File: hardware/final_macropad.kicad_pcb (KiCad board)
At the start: 4 copper layers, 91 x 91.8 mm, 65 parts, among them J1 OLED_128x64, SW1 SW_Push, U1 ATmega32U4-A, Y1 16MHz

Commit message: organize schematic and add USB-C and surge protector
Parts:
- removed R2, R3: 22, Resistor_SMD:R_0402_1005Metric_Pad0.72x0.64mm_HandSolder
- removed USB1: Molex-0548190589, random-keyboard-parts:Molex-0548190589
- added C10: 100nF, Capacitor_SMD:C_0805_2012Metric, F.Cu at (237.7, 42.0)
- added C11: 100nF, Capacitor_SMD:C_0805_2012Metric, F.Cu at (237.7, 45.1)
- added C8: 100nF, Capacitor_SMD:C_0805_2012Metric, F.Cu at (237.7, 36.0)
- added C9: 100nF, Capacitor_SMD:C_0805_2012Metric, F.Cu at (237.7, 39.0)
- added D1: SOD-123, Diode_SMD:D_SOD-123, F.Cu at (231.6, 101.7)
- added D10: SOD-123, Diode_SMD:D_SOD-123, F.Cu at (237.3, 111.8)
- added D11: SOD-123, Diode_SMD:D_SOD-123, F.Cu at (237.3, 115.1)
- added D12: SOD-123, Diode_SMD:D_SOD-123, F.Cu at (237.3, 118.5)
- added D13: SOD-123, Diode_SMD:D_SOD-123, F.Cu at (243.1, 101.7)
- added D14: SOD-123, Diode_SMD:D_SOD-123, F.Cu at (243.1, 105.0)
- added D15: SOD-123, Diode_SMD:D_SOD-123, F.Cu at (243.1, 108.4)
- added D16: SOD-123, Diode_SMD:D_SOD-123, F.Cu at (243.1, 111.8)
- added D2: SOD-123, Diode_SMD:D_SOD-123, F.Cu at (231.6, 105.0)
- added D3: SOD-123, Diode_SMD:D_SOD-123, F.Cu at (231.6, 108.4)
- added D4: SOD-123, Diode_SMD:D_SOD-123, F.Cu at (231.6, 111.8)
- added D5: SOD-123, Diode_SMD:D_SOD-123, F.Cu at (231.6, 115.1)
- added D6: SOD-123, Diode_SMD:D_SOD-123, F.Cu at (231.6, 118.5)
- added D7: SOD-123, Diode_SMD:D_SOD-123, F.Cu at (237.3, 101.7)
- added D8: SOD-123, Diode_SMD:D_SOD-123, F.Cu at (237.3, 105.0)
- added D9: SOD-123, Diode_SMD:D_SOD-123, F.Cu at (237.3, 108.4)
- added H10: OLED_Mount, MountingHole:MountingHole_2.2mm_M2_Pad, F.Cu at (228.1, 43.5)
- added H11: OLED_Mount, MountingHole:MountingHole_2.2mm_M2_Pad, F.Cu at (228.1, 49.4)
- added H12: OLED_Mount, MountingHole:MountingHole_2.2mm_M2_Pad, F.Cu at (228.1, 55.4)
- added H9: OLED_Mount, MountingHole:MountingHole_2.2mm_M2_Pad, F.Cu at (228.1, 37.5)
- added J2: 2137160001, kicad-footprints:MOLEX_2137160001, F.Cu at (138.1, 39.5)
- added J2: 2137160001, kicad-footprints:MOLEX_2137160001, F.Cu at (88.7, 25.9)
- added R10: 10k, Resistor_SMD:R_0805_2012Metric, F.Cu at (233.2, 50.8)
- added R11: 5.1k, Resistor_SMD:R_0805_2012Metric, F.Cu at (134.5, 42.2)
- added R11: 5.1k, Resistor_SMD:R_0805_2012Metric, F.Cu at (77.8, 30.0)
- added R12: 5.1k, Resistor_SMD:R_0805_2012Metric, F.Cu at (134.5, 45.2)
- added R12: 5.1k, Resistor_SMD:R_0805_2012Metric, F.Cu at (77.8, 33.0)
- added R5: 27k, Resistor_SMD:R_0805_2012Metric, F.Cu at (233.2, 36.0)
- added R6: 27k, Resistor_SMD:R_0805_2012Metric, F.Cu at (233.2, 39.0)
- added R7: 10k, Resistor_SMD:R_0805_2012Metric, F.Cu at (233.2, 41.9)
- added R8: 27k, Resistor_SMD:R_0805_2012Metric, F.Cu at (233.2, 44.9)
- added R9: 27k, Resistor_SMD:R_0805_2012Metric, F.Cu at (233.2, 47.8)
- added S15: Keyswitch, Button_Switch_Keyboard:SW_Cherry_MX_1.00u_PCB, F.Cu at (105.5, 64.8)
- added S16: Keyswitch, Button_Switch_Keyboard:SW_Cherry_MX_1.00u_PCB, F.Cu at (105.5, 84.0)
- added S17: Keyswitch, Button_Switch_Keyboard:SW_Cherry_MX_1.00u_PCB, F.Cu at (105.5, 103.2)
- added S18: Keyswitch, Button_Switch_Keyboard:SW_Cherry_MX_1.00u_PCB, F.Cu at (105.5, 122.5)
- added U2: USBLC6-2SC6, kicad-footprints:SOT95P280X145-6N, F.Cu at (140.0, 43.0)
- added U2: USBLC6-2SC6, kicad-footprints:SOT95P280X145-6N, F.Cu at (68.3, 33.5)
- F1: moved to F.Cu
- H1, H2, H3, H4, H5, H6, H7, H8: value MountingHole_Pad -> MountHole
- S13: footprint PEC16-4220F-S0024:PEC16-4xxxx-Sxxxx -> kicad-footprints:PEC16-4xxxx-Sxxxx
- moved F1 82.8 mm to (145.4, 42.4), turned to 0 degrees
- moved S4 82.5 mm to (47.8, 122.5)
- moved S14 81.6 mm to (155.2, 66.8)
- moved S13 80.6 mm to (179.5, 65.5)
- moved S8 55.3 mm to (67.0, 122.5)
- moved S3 55.2 mm to (47.8, 103.2)
- moved S9 53.8 mm to (86.2, 64.8)
- moved J1 39.3 mm to (10.4, 26.8)
- moved S7 28.0 mm to (67.0, 103.2)
- moved S12 28.0 mm to (86.2, 122.5)
- moved S2 28.0 mm to (47.8, 84.0)
- moved S5 26.5 mm to (67.0, 64.8)
- moved S10 26.5 mm to (86.2, 84.0)
- moved H3 25.8 mm to (32.5, 140.1)
- moved H4 25.8 mm to (114.5, 140.1)
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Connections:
- U1 pad 27: unconnected-(U1-PD7-Pad27) -> ROW 3
- U1 pad 3: /CAPD- -> MPU_USB_D-
- U1 pad 4: /CAPD+ -> MPU_USB_D+
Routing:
- net COL 2: track 83.3 -> 44.7 mm
- net COL 0: track 57.4 -> 18.9 mm
- net COL 3: track 101.4 -> 62.9 mm
- net COL 1: track 66.5 -> 28.1 mm
- net /CAPD+: track 16.8 -> 0.00 mm
- net /CAPD-: track 16.8 -> 0.00 mm
- net Net-(D5-A): track 14.3 -> 0.00 mm
- net 5V: track 33.9 -> 27.2 mm, vias 7 -> 6
- net VCC: track 5.24 -> 0.00 mm
- net D+: track 2.91 -> 0.00 mm
- net D-: track 2.89 -> 0.00 mm
- net ROW 1: track 105.4 -> 102.9 mm
- net GND: track 51.0 -> 50.7 mm, vias 12 -> 10
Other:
- board size 91 x 91.8 mm -> 91.2 x 118 mm

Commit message: remove old diodes
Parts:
- removed the D1 at (54.8, 67.5)
- removed the D10 at (74.0, 107.2)
- removed the D11 at (93.2, 107.2)
- removed the D12 at (112.8, 107.2)
- removed the D2 at (73.8, 67.5)
- removed the D3 at (93.0, 67.5)
- removed the D4 at (112.5, 67.5)
- removed the D5 at (54.5, 89.2)
- removed the D6 at (73.8, 89.2)
- removed the D7 at (93.2, 89.2)
- removed the D8 at (112.5, 89.2)
- removed the D9 at (54.5, 107.2)
- moved D1 230.0 mm to (5.05, 61.5)
- moved D10 230.0 mm to (10.8, 71.6)
- moved D11 230.0 mm to (10.8, 75.0)
- moved D12 230.0 mm to (10.8, 78.3)
- moved D13 230.0 mm to (16.6, 61.5)
- moved D14 230.0 mm to (16.6, 64.9)
- moved D15 230.0 mm to (16.6, 68.2)
- moved D16 230.0 mm to (16.6, 71.6)
- moved D2 230.0 mm to (5.05, 64.9)
- moved D3 230.0 mm to (5.05, 68.2)
- moved D4 230.0 mm to (5.05, 71.6)
- moved D5 230.0 mm to (5.05, 75.0)
- moved D6 230.0 mm to (5.05, 78.3)
- moved D7 230.0 mm to (10.8, 61.5)
- moved D8 230.0 mm to (10.8, 64.9)
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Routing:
- net COL 0: track 18.9 -> 32.5 mm
- net Net-(D1-A): track 13.7 -> 0.00 mm

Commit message: fix switches to be correct order and move diodes
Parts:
- D1, D10, D11, D12, D13, D14, D15, D16, D2, D3, D4, D5, D6, D7, D8, D9: moved to B.Cu
- H5, H6, H7, H8: footprint MountingHole:MountingHole_3.2mm_M3_Pad_Via -> MountingHole:MountingHole_2.2mm_M2_Pad
- moved D16 110.8 mm to (112.5, 127.2), turned to 90 degrees
- moved D4 107.5 mm to (112.5, 68.5), turned to 90 degrees
- moved D12 105.9 mm to (112.5, 107.8), turned to 90 degrees
- moved D8 104.2 mm to (112.5, 88.0), turned to 90 degrees
- moved D15 96.9 mm to (93.5, 127.2), turned to 90 degrees
- moved D11 88.7 mm to (93.2, 107.8), turned to 90 degrees
- moved D3 88.4 mm to (93.5, 68.5), turned to 90 degrees
- moved D7 86.8 mm to (93.5, 88.0), turned to 90 degrees
- moved D14 84.9 mm to (74.2, 127.2), turned to 90 degrees
- moved C10 84.3 mm to (156.1, 63.2)
- moved C11 84.3 mm to (156.1, 66.2)
- moved C8 84.3 mm to (156.1, 57.2)
- moved C9 84.3 mm to (156.1, 60.2)
- moved H10 84.3 mm to (146.5, 64.6)
- moved H11 84.3 mm to (146.5, 70.5)
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- renumbered S15 to S13, S16 to S14, S17 to S15, S18 to S16, S13 to S17, S14 to S18
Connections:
- R5 pad 2: Net-(S13-CHANNEL_A) -> Net-(S17-CHANNEL_A)
- R6 pad 2: Net-(S13-CHANNEL_B) -> Net-(S17-CHANNEL_B)
- R8 pad 2: Net-(S14-CHANNEL_A) -> Net-(S18-CHANNEL_A)
- R9 pad 2: Net-(S14-CHANNEL_B) -> Net-(S18-CHANNEL_B)
- S17 pad A: Net-(S13-CHANNEL_A) -> Net-(S17-CHANNEL_A)
- S17 pad B: Net-(S13-CHANNEL_B) -> Net-(S17-CHANNEL_B)
- S18 pad A: Net-(S14-CHANNEL_A) -> Net-(S18-CHANNEL_A)
- S18 pad B: Net-(S14-CHANNEL_B) -> Net-(S18-CHANNEL_B)
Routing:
- net ROW 2: track 141.0 -> 37.7 mm, vias 2 -> 1
- net ROW 1: track 102.9 -> 19.9 mm, vias 2 -> 1
- net ROW 0: track 92.0 -> 19.6 mm, vias 2 -> 1
- net Net-(D7-A): track 14.5 -> 0.00 mm
- net SDA: track 18.2 -> 3.70 mm
- net Net-(D8-A): track 14.5 -> 0.00 mm
- net Net-(D6-A): track 14.3 -> 0.00 mm
- net Net-(D12-A): track 14.2 -> 0.00 mm
- net Net-(D10-A): track 14.0 -> 0.00 mm
- net Net-(D11-A): track 13.9 -> 0.00 mm
- net Net-(D9-A): track 13.8 -> 0.00 mm
- net COL 0: track 32.5 -> 18.9 mm
- net Net-(D4-A): track 13.6 -> 0.00 mm
- net Net-(D2-A): track 13.4 -> 0.00 mm
- net Net-(D3-A): track 13.3 -> 0.00 mm
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
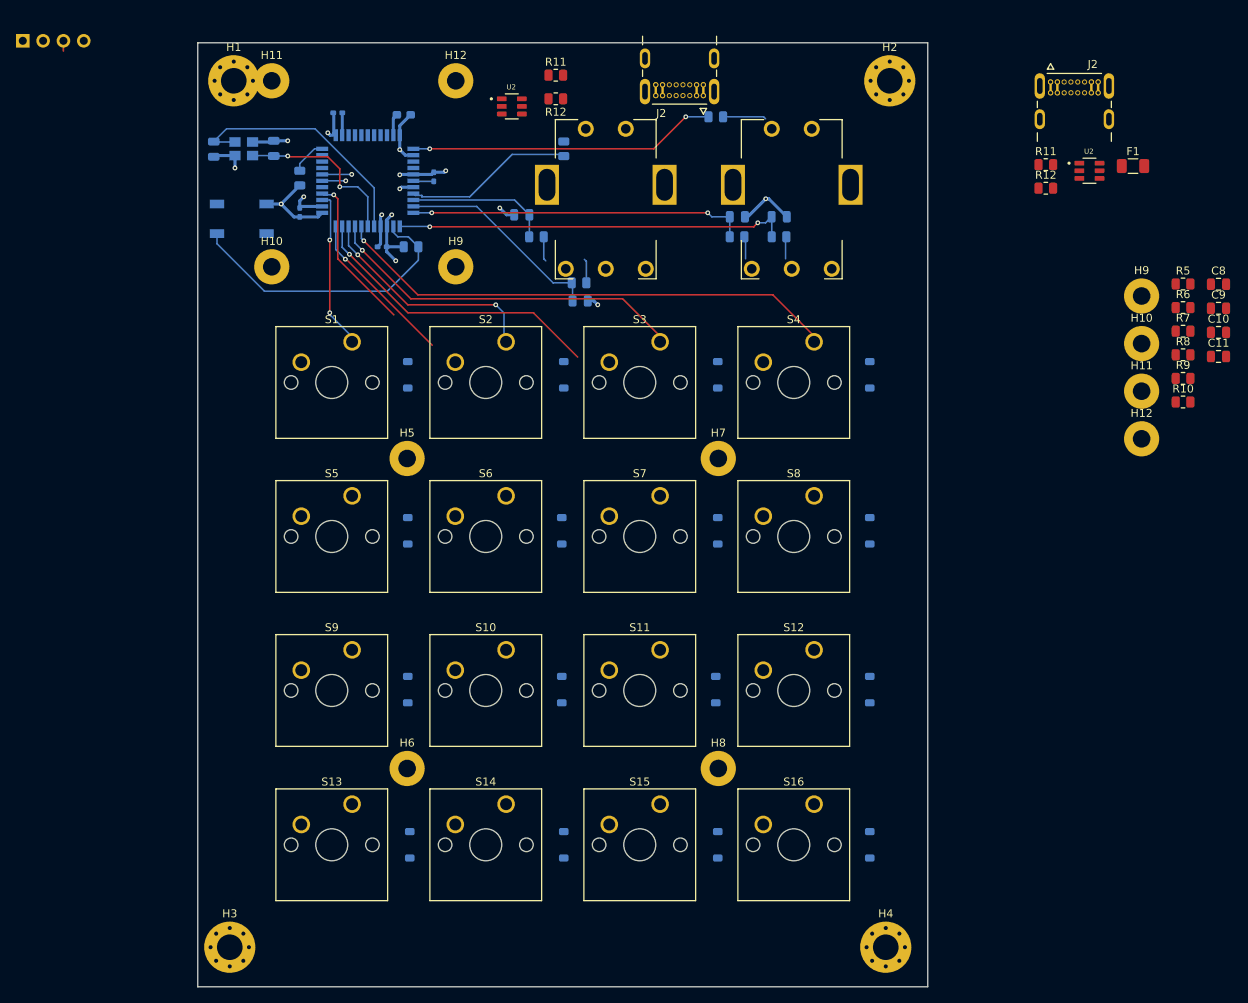
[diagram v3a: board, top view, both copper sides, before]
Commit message: route USBC connector
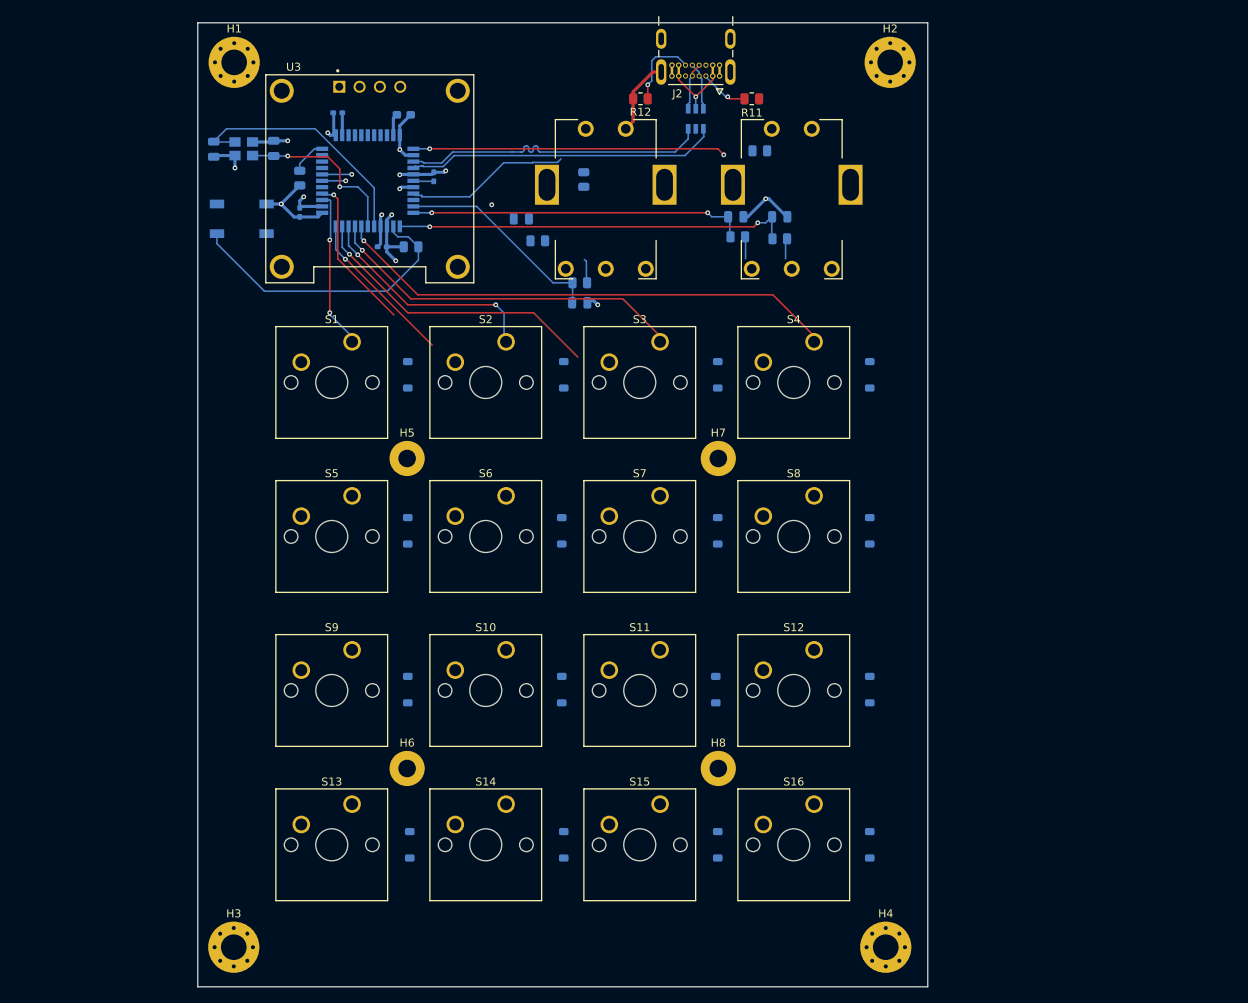
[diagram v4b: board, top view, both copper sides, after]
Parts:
- removed the C10 at (156.1, 63.2)
- removed the C10 at (69.0, 48.5)
- removed the C11 at (156.1, 66.2)
- removed the C11 at (76.3, 59.2)
- removed the C8 at (156.1, 57.2)
- removed the C8 at (96.0, 48.8)
- removed the C9 at (156.1, 60.2)
- removed the C9 at (101.2, 48.8)
- removed F1: 500mA, Fuse:Fuse_1206_3216Metric
- removed H10 (x2), H11 (x2), H12 (x2), H9 (x2): OLED_Mount, MountingHole:MountingHole_2.2mm_M2_Pad
- removed J1: OLED_128x64, ScottoKeebs_Components:OLED_128x64
- removed the J2 at (138.1, 39.5)
- removed the J2 at (88.7, 25.9)
- removed the R10 at (151.7, 71.9)
- removed the R10 at (74.2, 40.2)
- removed the R11 at (134.5, 42.2)
- removed the R11 at (73.2, 31.1)
- removed the R12 at (134.5, 45.2)
- removed the R12 at (73.2, 34.0)
- removed the R5 at (151.7, 57.1)
- removed the R5 at (95.9, 51.2)
- removed the R6 at (151.7, 60.1)
- removed the R6 at (101.2, 51.2)
- removed the R7 at (151.7, 63.0)
- removed the R7 at (93.2, 36.2)
- removed the R8 at (151.7, 66.0)
- removed the R8 at (70.8, 51.2)
- removed the R9 at (151.7, 69.0)
- removed the R9 at (76.2, 57.0)
- removed the U2 at (140.0, 43.0)
- removed the U2 at (67.8, 35.0)
- added C10: 100nF, Capacitor_SMD:C_0805_2012Metric, B.Cu at (69.0, 49.0)
- added C11: 100nF, Capacitor_SMD:C_0805_2012Metric, B.Cu at (76.2, 59.5)
- added C8: 100nF, Capacitor_SMD:C_0805_2012Metric, B.Cu at (95.8, 48.8)
- added C9: 100nF, Capacitor_SMD:C_0805_2012Metric, B.Cu at (101.2, 48.8)
- added J2: 2137160001, kicad-footprints:MOLEX_2137160001, F.Cu at (90.8, 23.5)
- added R10: 10k, Resistor_SMD:R_0805_2012Metric, B.Cu at (76.8, 44.1)
- added R11: 5.1k, Resistor_SMD:R_0805_2012Metric, F.Cu at (97.8, 34.0)
- added R12: 5.1k, Resistor_SMD:R_0805_2012Metric, F.Cu at (83.8, 34.0)
- added R5: 27k, Resistor_SMD:R_0805_2012Metric, B.Cu at (96.0, 51.2)
- added R6: 27k, Resistor_SMD:R_0805_2012Metric, B.Cu at (101.2, 51.5)
- added R7: 10k, Resistor_SMD:R_0805_2012Metric, B.Cu at (98.8, 40.5)
- added R8: 27k, Resistor_SMD:R_0805_2012Metric, B.Cu at (71.0, 51.8)
- added R9: 27k, Resistor_SMD:R_0805_2012Metric, B.Cu at (76.2, 57.0)
- added U2: USBLC6-2SC6, kicad-footprints:SOT95P280X145-6N, B.Cu at (90.8, 36.5)
- added U3: DM-OLED096-636, kicad-footprints:MODULE_DM-OLED096-636, F.Cu at (50.0, 44.0)
- moved H1 2.30 mm to (33.1, 29.4)
- moved H2 2.30 mm to (115.1, 29.4)
- moved H3 0.50 mm to (33.0, 140.1)
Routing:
- net MPU_USB_D+: track 0.00 -> 39.1 mm
- net MPU_USB_D-: track 0.00 -> 39.0 mm
- net ROTA1: track 18.0 -> 0.00 mm
- net ROTB0: track 49.5 -> 59.4 mm, vias 2 -> 3
- net Net-(J2-CC2): track 0.00 -> 9.86 mm, vias 0 -> 1
- net VBUS+: track 0.00 -> 8.46 mm, vias 0 -> 2
- net Net-(J2-CC1): track 0.00 -> 6.07 mm, vias 0 -> 1
- net USB_D+: track 0.00 -> 6.01 mm
- net USB_D-: track 0.00 -> 6.01 mm
- net Net-(R7-Pad2): track 5.42 -> 0.00 mm
- net Net-(S14-CHANNEL_A): track 3.10 -> 0.00 mm
- net Net-(S18-CHANNEL_B): track 0.00 -> 3.03 mm
- net Net-(S14-CHANNEL_B): track 3.03 -> 0.00 mm
- net Net-(S17-CHANNEL_A): track 0.00 -> 2.81 mm
- net Net-(S13-CHANNEL_A): track 2.81 -> 0.00 mm
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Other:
- board size 91.2 x 118 mm -> 91.2 x 120.5 mm

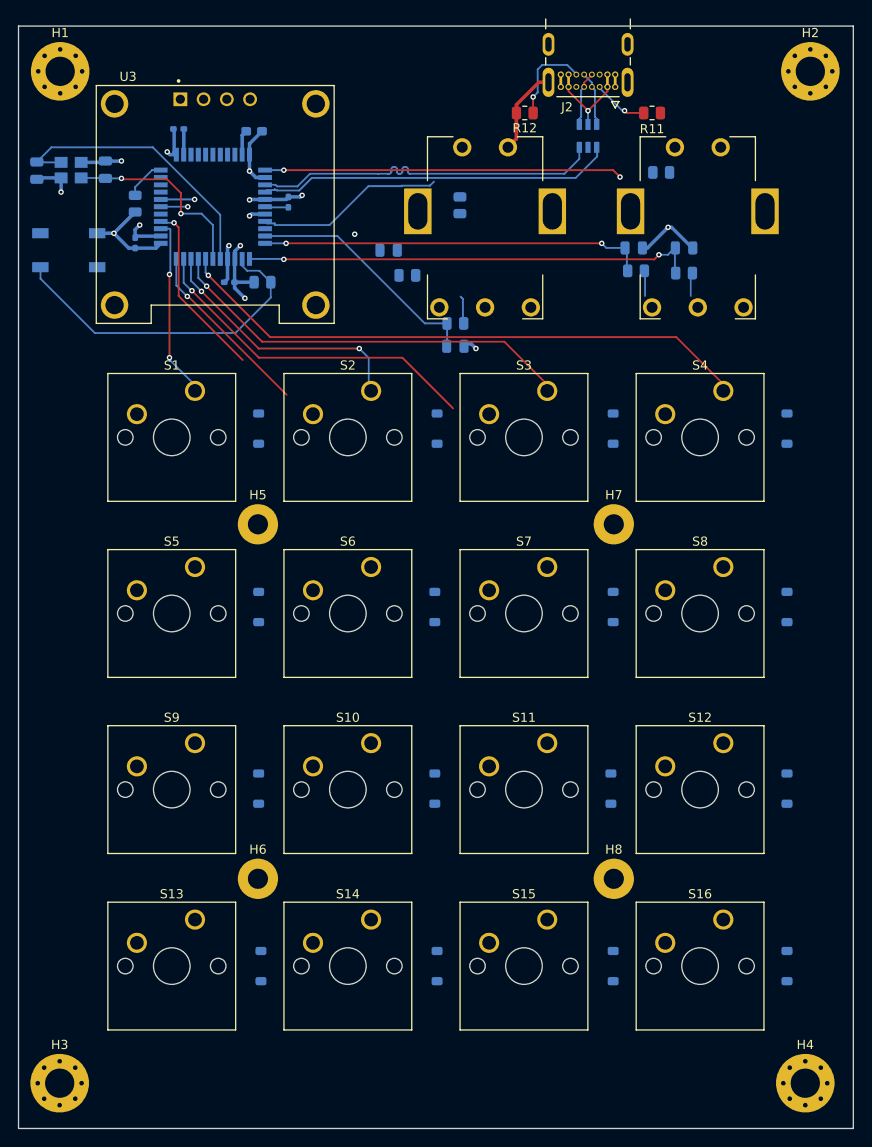
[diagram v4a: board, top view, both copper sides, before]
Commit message: route USB and rotary encoder
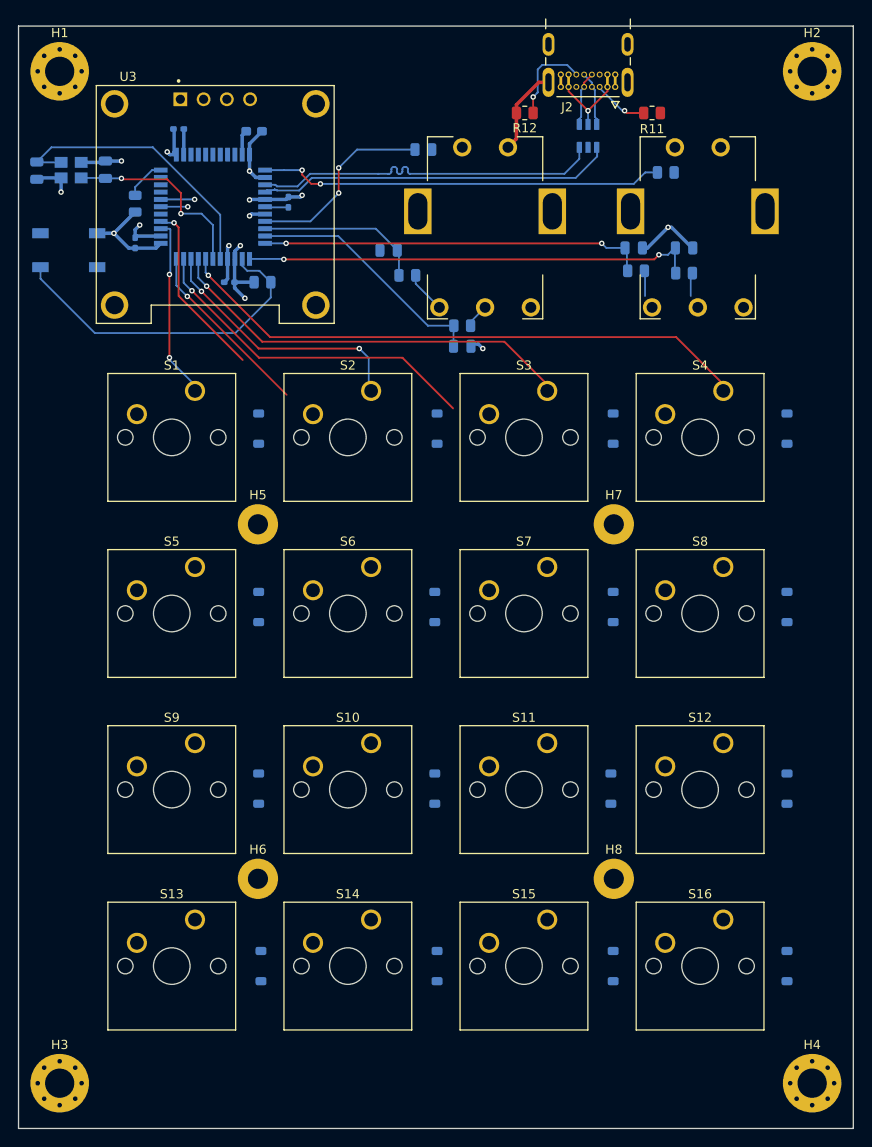
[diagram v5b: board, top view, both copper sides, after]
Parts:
- moved R10 7.28 mm to (72.8, 38.0), turned to 0 degrees
- moved R9 0.79 mm to (77.0, 57.2)
- moved C11 0.75 mm to (77.0, 59.5)
- moved H4 0.75 mm to (115.2, 140.1)
- moved R7 0.50 mm to (99.2, 40.5)
- moved H2 0.20 mm to (115.2, 29.4)
- moved H1 0.05 mm to (33.0, 29.4)
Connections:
- U3 pad S1: (no net) -> GND
- U3 pad S2: (no net) -> GND
- U3 pad S3: (no net) -> GND
- U3 pad S4: (no net) -> GND
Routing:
- net ROTA1: track 0.00 -> 18.3 mm
- net SW0: track 39.1 -> 43.8 mm
- net Net-(S18-CHANNEL_A): track 0.00 -> 4.57 mm
- net ROTB1: track 26.0 -> 27.0 mm
- net SW1: track 20.7 -> 21.2 mm, vias 0 -> 2
- net GND: vias 8 -> 7
